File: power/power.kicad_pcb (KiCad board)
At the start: 4 copper layers, 57.2 x 39.4 mm, 71 parts, among them M1 HIP2101, M2 HIP2101, M3 HIP2101, M4 ACS711, M5 ACS711, P1 PLS_10, P2 PLS_3, P3 PLS_3, P4 C, P5 A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

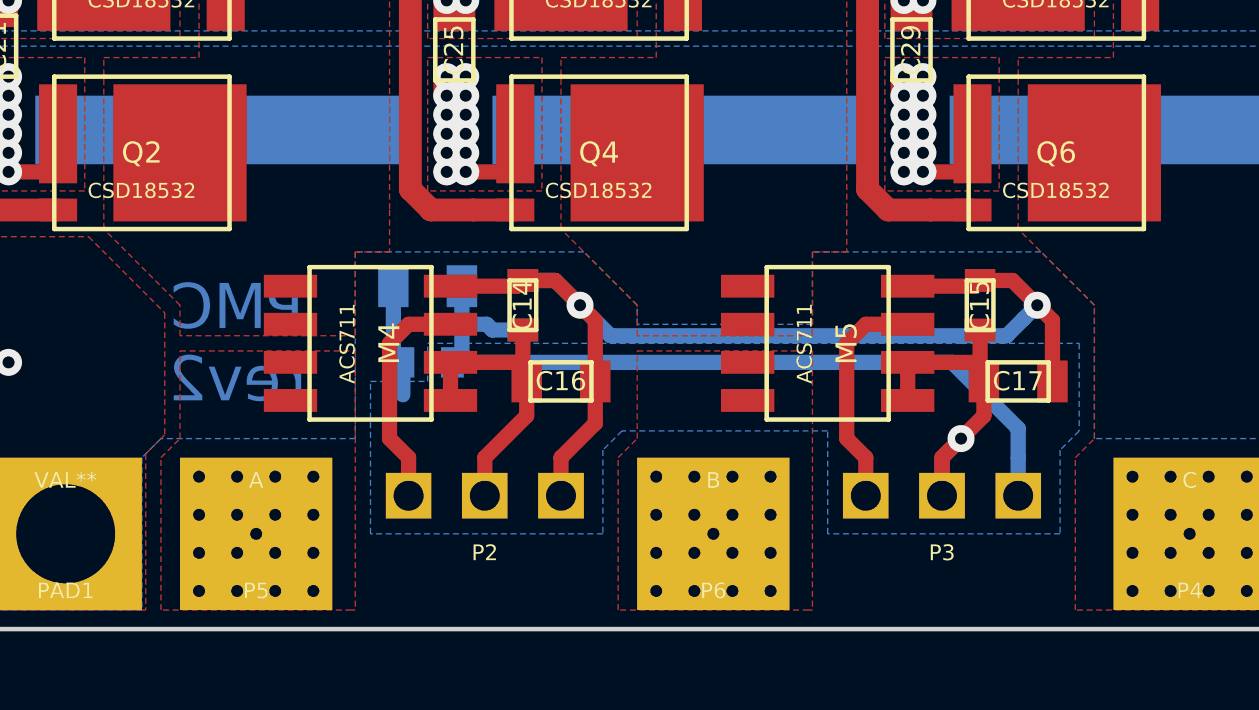
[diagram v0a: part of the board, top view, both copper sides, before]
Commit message: Replaced ACS7XX sensors to the current shunt amplifiers.
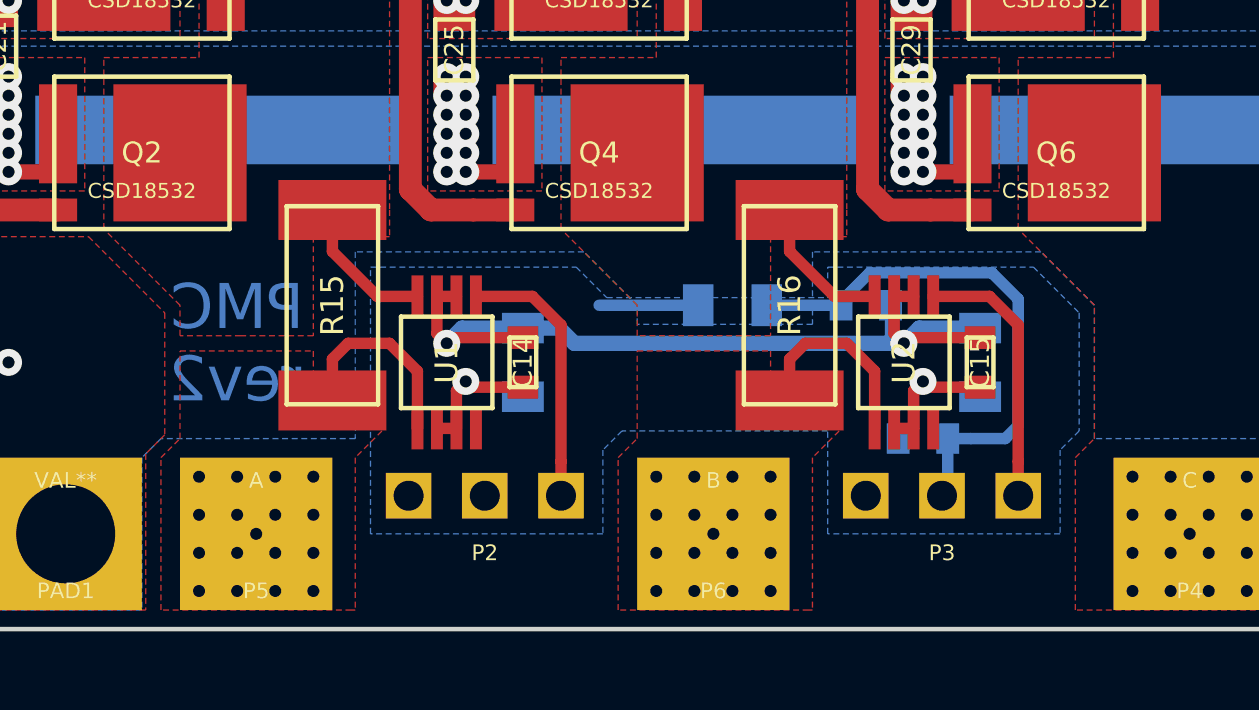
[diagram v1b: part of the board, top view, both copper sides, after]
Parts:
- removed M4, M5: ACS711, foot:SO8
- added R15: 0.0005, foot:LR2512, F.Cu at (162.6, 110.5)
- added R16: 0.0005, foot:LR2512, F.Cu at (177.8, 110.5)
- added U1: AD8417, foot:MSOP8, F.Cu at (166.4, 112.4)
- added U2: AD8417, foot:MSOP8, F.Cu at (181.6, 112.4)
- C16, C17: moved to B.Cu
- moved C7 16.7 mm to (182.2, 114.9)
- moved R7 11.4 mm to (180.3, 110.5), turned to 0 degrees
- moved R8 10.2 mm to (175.9, 110.5)
- moved C14 1.91 mm to (168.9, 112.4), turned to 90 degrees
- moved C15 1.91 mm to (184.2, 112.4), turned to 90 degrees
- moved C16 1.42 mm to (168.9, 112.4), turned to 270 degrees
- moved C17 1.42 mm to (184.2, 112.4), turned to 270 degrees
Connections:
- C14 pad 1: +3.3V -> AGND
- C14 pad 2: AGND -> +3.3V
- C15 pad 1: +3.3V -> AGND
- C15 pad 2: AGND -> +3.3V
- P2 pad 1: SENSOR_A -> AGND
- P2 pad 2: AGND -> +3.3V
- P2 pad 3: +3.3V -> SENSOR_A
- P3 pad 1: SENSOR_B -> AGND
- P3 pad 2: AGND -> SENSOR_NTC
- P3 pad 3: SENSOR_NTC -> SENSOR_B
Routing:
- net AGND: track 25.4 -> 12.0 mm, vias 1 -> 2
- net SENSOR_NTC: track 26.8 -> 18.0 mm
- net +3.3V: track 37.6 -> 29.7 mm
- net Net-(P5-Pad1): track 19.1 -> 26.3 mm
- net Net-(P6-Pad1): track 19.1 -> 25.8 mm
- net Net-(C8-Pad1): track 17.0 -> 21.8 mm
- net Net-(C10-Pad1): track 17.0 -> 21.8 mm
- net SENSOR_B: track 7.64 -> 8.92 mm
- net SENSOR_A: track 7.64 -> 8.92 mm
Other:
- net class Default: clearance 0.381 -> 0.2
- rule trace_clearance: 0.381 -> 0.2

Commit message: Small fixes for rev2.
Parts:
- moved R7 0.90 mm to (179.7, 111.1), turned to 270 degrees
- moved C16 0.63 mm to (168.9, 111.8)
- moved C17 0.63 mm to (184.2, 111.8)
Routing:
- net AGND: track 12.0 -> 12.9 mm
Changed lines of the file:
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@@
   (title_block
     (title "Phobia Power Board")
-    (date 2016-03-31)
+    (date 2016-09-21)
     (rev 2)
     (company "Roman Belov")
@@
   )
   (setup
-    (last_trace_width 0.381)
+    (last_trace_width 0.508)
     (user_trace_width 0.381)
     (user_trace_width 0.762)
@@
   )
   (module foot:SM0805 (layer B.Cu)
-    (at 168.91 112.395 270)
+    (at 168.91 111.76 270)
     (attr smd)
     (fp_text reference C16 (at 0 0 270) (layer B.SilkS)
@@
   )
   (module foot:SM0805 (layer B.Cu)
-    (at 184.15 112.395 270)
+    (at 184.15 111.76 270)
     (attr smd)
     (fp_text reference C17 (at 0 0 270) (layer B.SilkS)
@@
   )
   (module foot:SM0603 (layer B.Cu)
-    (at 180.34 110.49)
-    (attr smd)
-    (fp_text reference R7 (at 0 0) (layer B.SilkS)
-      (effects (font (size 0.635 0.635) (thickness 0.127)) (justify mirror))
-    )
-    (fp_text value 10K (at 0 1.397) (layer B.SilkS) hide
+    (at 179.705 111.125 270)
+    (attr smd)
+    (fp_text reference R7 (at 0 0 270) (layer B.SilkS)
+      (effects (font (size 0.635 0.635) (thickness 0.127)) (justify mirror))
+    )
+    (fp_text value 10K (at 0 1.397 270) (layer B.SilkS) hide
       (effects (font (size 0.635 0.635) (thickness 0.127)) (justify mirror))
     )
@@
     (fp_line (start -0.8255 -0.4445) (end -0.8255 0.4445) (layer B.SilkS) (width 0.15))
     (fp_line (start -0.8255 0.4445) (end 0.8255 0.4445) (layer B.SilkS) (width 0.15))
-    (pad 1 smd rect (at -0.8255 0) (size 0.762 1.016) (layers B.Cu B.Paste B.Mask)
+    (pad 1 smd rect (at -0.8255 0 270) (size 0.762 1.016) (layers B.Cu B.Paste B.Mask)
       (net 28 SENSOR_NTC))
-    (pad 2 smd rect (at 0.8255 0) (size 0.762 1.016) (layers B.Cu B.Paste B.Mask)
+    (pad 2 smd rect (at 0.8255 0 270) (size 0.762 1.016) (layers B.Cu B.Paste B.Mask)
       (net 5 +3.3V))
   )
@@
   (segment (start 174.117 92.075) (end 176.53 92.075) (width 0.762) (layer F.Cu) (net 4))
   (segment (start 176.53 92.583) (end 176.657 92.71) (width 0.762) (layer F.Cu) (net 4))
-  (segment (start 170.6245 111.76) (end 180.975 111.76) (width 0.508) (layer B.Cu) (net 5))
-  (segment (start 180.975 111.76) (end 181.61 111.76) (width 0.508) (layer B.Cu) (net 5))
-  (segment (start 181.1655 110.49) (end 181.1655 111.5695) (width 0.381) (layer B.Cu) (net 5))
-  (segment (start 181.1655 111.5695) (end 180.975 111.76) (width 0.381) (layer B.Cu) (net 5))
-  (segment (start 184.15 111.252) (end 182.118 111.252) (width 0.508) (layer B.Cu) (net 5))
-  (segment (start 182.118 111.252) (end 181.61 111.76) (width 0.508) (layer B.Cu) (net 5))
-  (segment (start 168.91 111.252) (end 170.1165 111.252) (width 0.508) (layer B.Cu) (net 5))
-  (segment (start 170.1165 111.252) (end 170.6245 111.76) (width 0.508) (layer B.Cu) (net 5))
-  (segment (start 168.91 111.252) (end 166.878 111.252) (width 0.508) (layer B.Cu) (net 5))
-  (segment (start 166.878 111.252) (end 166.37 111.76) (width 0.508) (layer B.Cu) (net 5))
+  (segment (start 168.91 110.617) (end 167.513 110.617) (width 0.508) (layer B.Cu) (net 5))
+  (segment (start 167.513 110.617) (end 166.37 111.76) (width 0.508) (layer B.Cu) (net 5))
+  (segment (start 168.91 110.617) (end 170.1165 110.617) (width 0.508) (layer B.Cu) (net 5))
+  (segment (start 170.1165 110.617) (end 171.45 111.9505) (width 0.508) (layer B.Cu) (net 5))
+  (segment (start 171.45 111.9505) (end 178.689 111.9505) (width 0.508) (layer B.Cu) (net 5))
+  (segment (start 178.689 111.9505) (end 179.705 111.9505) (width 0.508) (layer B.Cu) (net 5))
+  (segment (start 184.15 110.617) (end 182.753 110.617) (width 0.508) (layer B.Cu) (net 5))
+  (segment (start 182.753 110.617) (end 181.61 111.76) (width 0.508) (layer B.Cu) (net 5))
+  (via (at 166.37 111.76) (size 0.9) (drill 0.4) (layers F.Cu B.Cu) (net 5))
+  (segment (start 179.705 111.9505) (end 181.4195 111.9505) (width 0.508) (layer B.Cu) (net 5))
+  (segment (start 181.4195 111.9505) (end 181.61 111.76) (width 0.508) (layer B.Cu) (net 5))
   (segment (start 166.045 110.195) (end 166.045 111.435) (width 0.381) (layer F.Cu) (net 5))
   (segment (start 166.045 111.435) (end 166.37 111.76) (width 0.381) (layer F.Cu) (net 5))
   (segment (start 168.91 111.5695) (end 166.5605 111.5695) (width 0.381) (layer F.Cu) (net 5))
   (segment (start 166.5605 111.5695) (end 166.37 111.76) (width 0.381) (layer F.Cu) (net 5))
-  (via (at 166.37 111.76) (size 0.9) (drill 0.4) (layers F.Cu B.Cu) (net 5))
   (segment (start 181.285 110.195) (end 181.285 111.435) (width 0.381) (layer F.Cu) (net 5))
   (segment (start 181.285 111.435) (end 181.61 111.76) (width 0.381) (layer F.Cu) (net 5))
@@
   (segment (start 166.045 110.195) (end 166.695 110.195) (width 0.381) (layer F.Cu) (net 5))
   (segment (start 181.285 110.195) (end 181.935 110.195) (width 0.381) (layer F.Cu) (net 5))
+  (segment (start 171.45 110.49) (end 170.815 109.855) (width 0.381) (layer B.Cu) (net 6))
   (segment (start 174.752 110.49) (end 171.45 110.49) (width 0.381) (layer B.Cu) (net 6))
   (segment (start 166.695 114.595) (end 166.695 113.34) (width 0.381) (layer F.Cu) (net 6))
@@
   (segment (start 175.26 85.09) (end 175.26 83.82) (width 0.508) (layer F.Cu) (net 27))
   (segment (start 184.023 89.535) (end 184.023 89.408) (width 0.508) (layer F.Cu) (net 27))
+  (segment (start 177.038 110.49) (end 179.5145 110.49) (width 0.381) (layer B.Cu) (net 28))
+  (segment (start 179.5145 110.49) (end 179.705 110.2995) (width 0.381) (layer B.Cu) (net 28))
+  (segment (start 179.832 110.2995) (end 180.6575 109.474) (width 0.381) (layer B.Cu) (net 28))
+  (segment (start 185.42 109.977598) (end 185.42 114.3) (width 0.381) (layer B.Cu) (net 28))
+  (segment (start 180.6575 109.474) (end 184.916402 109.474) (width 0.381) (layer B.Cu) (net 28))
+  (segment (start 184.916402 109.474) (end 185.42 109.977598) (width 0.381) (layer B.Cu) (net 28))
+  (segment (start 185.42 114.3) (end 184.785 114.935) (width 0.381) (layer B.Cu) (net 28))
+  (segment (start 184.785 114.935) (end 183.0705 114.935) (width 0.381) (layer B.Cu) (net 28))
   (segment (start 183.0705 114.935) (end 183.0705 116.6495) (width 0.381) (layer B.Cu) (net 28))
   (segment (start 183.0705 116.6495) (end 182.88 116.84) (width 0.381) (layer B.Cu) (net 28))
-  (segment (start 179.5145 110.49) (end 179.5145 110.363) (width 0.381) (layer B.Cu) (net 28))
-  (segment (start 179.5145 110.363) (end 180.467001 109.410499) (width 0.381) (layer B.Cu) (net 28))
-  (segment (start 180.467001 109.410499) (end 184.543701 109.410499) (width 0.381) (layer B.Cu) (net 28))
-  (segment (start 184.543701 109.410499) (end 185.420001 110.286799) (width 0.381) (layer B.Cu) (net 28))
-  (segment (start 184.988202 114.935) (end 183.8325 114.935) (width 0.381) (layer B.Cu) (net 28))
-  (segment (start 185.420001 110.286799) (end 185.420001 114.503201) (width 0.381) (layer B.Cu) (net 28))
-  (segment (start 185.420001 114.503201) (end 184.988202 114.935) (width 0.381) (layer B.Cu) (net 28))
-  (segment (start 183.8325 114.935) (end 183.0705 114.935) (width 0.381) (layer B.Cu) (net 28))
-  (segment (start 177.038 110.49) (end 179.5145 110.49) (width 0.381) (layer B.Cu) (net 28))
   (segment (start 162.56 107.315) (end 162.56 108.69549) (width 0.381) (layer F.Cu) (net 29))
   (segment (start 162.56 108.69549) (end 164.05951 110.195) (width 0.381) (layer F.Cu) (net 29))
@@
     (polygon
       (pts
-        (xy 149.098 96.139) (xy 149.098 107.061) (xy 150.241 108.204) (xy 154.432 108.204) (xy 156.972 110.744)
+        (xy 149.098 96.012) (xy 149.098 107.061) (xy 150.241 108.204) (xy 154.432 108.204) (xy 156.972 110.744)
         (xy 156.972 114.808) (xy 156.337 115.443) (xy 156.337 120.65) (xy 150.495 120.65) (xy 139.7 120.65)
-        (xy 139.7 82.55) (xy 150.622 82.55) (xy 150.622 94.615)
+        (xy 139.7 82.55) (xy 150.622 82.55) (xy 150.622 94.488)
       )
     )
@@
     (polygon
       (pts
-        (xy 139.7 87.63) (xy 150.495 87.63) (xy 150.495 94.996) (xy 195.58 94.996) (xy 195.58 101.346)
+        (xy 139.7 87.63) (xy 150.622 87.63) (xy 150.622 94.996) (xy 195.58 94.996) (xy 195.58 101.346)
         (xy 139.7 101.346)
       )
@@
     (polygon
       (pts
-        (xy 139.7 87.63) (xy 150.622 87.63) (xy 150.622 94.615) (xy 149.098 96.139) (xy 149.098 101.6)
-        (xy 139.7 101.6)
+        (xy 139.7 88.011) (xy 150.622 88.011) (xy 150.622 94.488) (xy 149.098 96.012) (xy 149.098 101.346)
+        (xy 139.7 101.346)
       )
     )
@@
     (polygon
       (pts
-        (xy 139.7 115.57) (xy 150.495 115.57) (xy 150.495 120.65) (xy 139.7 120.65)
+        (xy 139.7 115.57) (xy 150.749 115.57) (xy 150.749 120.65) (xy 139.7 120.65)
       )
     )
@@
     (polygon
       (pts
-        (xy 150.495 120.65) (xy 139.7 120.65) (xy 139.7 115.57) (xy 150.495 115.57) (xy 150.495 120.65)
+        (xy 150.495 120.65) (xy 139.7 120.65) (xy 139.7 115.57) (xy 150.749 115.57) (xy 150.749 120.65)
       )
     )
@@
     (polygon
       (pts
-        (xy 139.7 82.55) (xy 150.495 82.55) (xy 150.495 87.63) (xy 139.7 87.63)
-      )
-    )
+        (xy 139.7 82.55) (xy 150.622 82.55) (xy 150.622 87.63) (xy 139.7 87.63)
+      )
+    )

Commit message: Added revison 3.
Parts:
- removed C16, C17: 1uF, foot:SM0805
- removed PAD1 (x3): VAL**, foot:PAD1
- removed R1, R2, R3, R4, R5, R6: 10K, foot:SM0603
- added VIA: , foot:PLS1, F.Cu at (153.7, 118.1)
- added VIA: , foot:PLS1, F.Cu at (193.0, 85.1)
- added VIA: , foot:PLS1, F.Cu at (153.7, 85.1)
- C21, C25, C29: value 0.1uF -> 100nF
- M1, M2, M3: value HIP2101 -> UCC27211A; footprint foot:SO8 -> foot:SON8
- R10, R11, R12, R13, R14, R9: value 2 -> 1
- R7: value 10K -> 10K 1%
- moved C7 4.43 mm to (184.2, 110.9), turned to 90 degrees
- moved C2 3.86 mm to (157.5, 92.1)
- moved C4 3.86 mm to (172.7, 92.1)
- moved C6 3.86 mm to (188.0, 92.1)
- moved C13 1.42 mm to (191.1, 91.4)
- moved C11 1.42 mm to (175.9, 91.4)
- moved C9 1.42 mm to (160.7, 91.4)
- moved R8 0.64 mm to (175.3, 110.5)
- moved M1 0.64 mm to (156.2, 92.1)
- moved M2 0.64 mm to (171.4, 92.1)
- moved M3 0.64 mm to (186.7, 92.1)
- moved C10 0.63 mm to (177.8, 92.1), turned to 270 degrees
- moved C12 0.63 mm to (193.0, 92.1), turned to 270 degrees
- moved C8 0.63 mm to (162.6, 92.1), turned to 270 degrees
- moved R7 0.19 mm to (179.7, 110.9)
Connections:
- P1 pad 1: PGND -> +36V
- P1 pad 10: PGND -> +12V
- P1 pad 2: +36V -> PGND
- P1 pad 3: FET_AH -> FET_AL
- P1 pad 4: FET_AL -> FET_AH
- P1 pad 5: FET_BH -> FET_BL
- P1 pad 6: FET_BL -> FET_BH
- P1 pad 7: FET_CH -> FET_CL
- P1 pad 8: FET_CL -> FET_CH
- P1 pad 9: +12V -> PGND
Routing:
- net +12V: track 27.3 -> 66.6 mm
- net +36V: track 85.3 -> 60.1 mm
- net PGND: track 82.6 -> 70.2 mm, vias 65 -> 62
- net AGND: track 12.9 -> 24.0 mm
- net +3.3V: track 29.3 -> 25.2 mm
- net FET_CH: track 14.9 -> 11.3 mm
- net FET_CL: track 16.9 -> 13.4 mm
- net FET_BL: track 11.8 -> 9.24 mm
- net FET_AL: track 20.1 -> 17.7 mm
- net Net-(M3-Pad3): track 11.2 -> 8.86 mm
- net Net-(M1-Pad3): track 11.2 -> 8.86 mm
- net Net-(M2-Pad3): track 11.2 -> 8.86 mm
- net FET_BH: track 9.15 -> 8.41 mm
- net Net-(C10-Pad1): track 21.8 -> 21.1 mm
- net Net-(C12-Pad1): track 36.0 -> 35.3 mm
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- removed copper zone on In2.Cu, net +12V
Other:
- board text added: "PMC rev3"
- board text added: "R3"
- board text removed: "PMC rev2"
